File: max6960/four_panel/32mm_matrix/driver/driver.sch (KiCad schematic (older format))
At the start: 20 parts, among them M1 LED-MATRIX-8X8, M2 LED-MATRIX-8X8, M3 LED-MATRIX-8X8, M4 LED-MATRIX-8X8, P1 CONN_2X2, U1 MAX6960, U2 74AHC1G126, U3 MAX6960, U4 CONN15, U5 CONN15

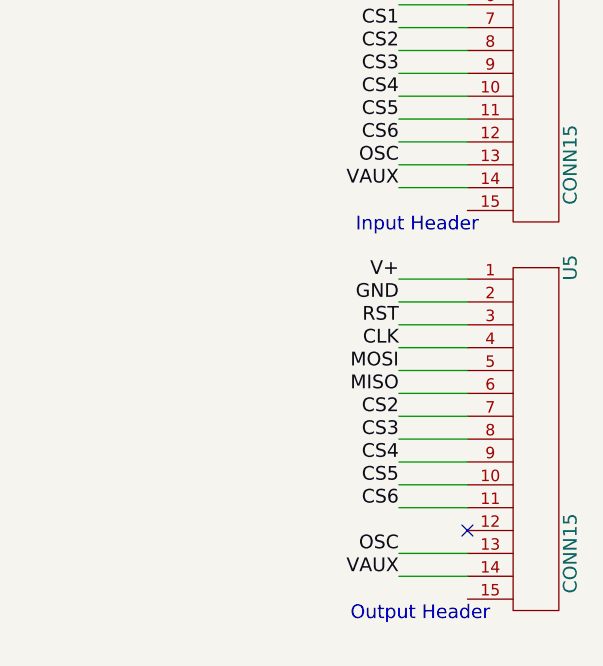
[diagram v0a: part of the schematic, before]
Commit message: Fixed errors in four panel 32mm matrix driver.
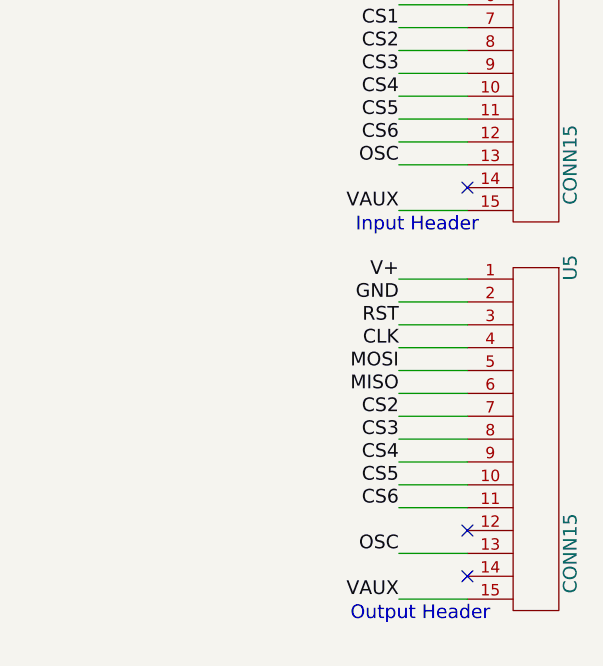
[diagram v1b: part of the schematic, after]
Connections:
- net VAUX: now also U4.15, U5.15; no longer U4.14, U5.14
- no-connect marks 2 -> 4
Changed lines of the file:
@@
-EESchema Schematic File Version 2  date Fri 26 Jul 2013 12:54:03 PM PDT
+EESchema Schematic File Version 2
 LIBS:power
 LIBS:device
@@
 LIBS:74ahc1g126
 LIBS:driver-cache
-EELAYER 25  0
+EELAYER 24 0
 EELAYER END
 $Descr User 18000 12000
@@
 	16100 7800 15800 7800
 Wire Wire Line
-	16100 7900 15800 7900
+	16100 8000 15800 8000
 Wire Wire Line
 	16100 8400 15800 8400
@@
 	16100 9200 15800 9200
 Wire Wire Line
-	16100 9600 15800 9600
+	16100 9700 15800 9700
 Wire Wire Line
 	11400 7450 10800 7450
@@
 F 0 "#PWR01" H 12850 9850 30  0001 C CNN
 F 1 "GND" H 12850 9780 30  0001 C CNN
+F 2 "" H 12850 9850 60  0001 C CNN
+F 3 "" H 12850 9850 60  0001 C CNN
 	1    12850 9850
 	1    0    0    -1
@@
 F 0 "P1" H 12300 9700 50  0000 C CNN
 F 1 "CONN_2X2" H 12310 9420 40  0000 C CNN
+F 2 "" H 12300 9550 60  0001 C CNN
+F 3 "" H 12300 9550 60  0001 C CNN
 	1    12300 9550
 	1    0    0    -1
@@
 F 0 "#PWR02" H 12850 8350 30  0001 C CNN
 F 1 "GND" H 12850 8280 30  0001 C CNN
+F 2 "" H 12850 8350 60  0001 C CNN
+F 3 "" H 12850 8350 60  0001 C CNN
 	1    12850 8350
 	1    0    0    -1
@@
 F 0 "C10" H 12900 8100 50  0000 L CNN
 F 1 "0.1uF" H 12900 7900 50  0000 L CNN
+F 2 "" H 12850 8000 60  0001 C CNN
+F 3 "" H 12850 8000 60  0001 C CNN
 	1    12850 8000
 	1    0    0    -1
@@
 F 0 "#PWR03" H 11250 7800 30  0001 C CNN
 F 1 "GND" H 11250 7730 30  0001 C CNN
+F 2 "" H 11250 7800 60  0001 C CNN
+F 3 "" H 11250 7800 60  0001 C CNN
 	1    11250 7800
 	1    0    0    -1
@@
 F 0 "U2" H 11750 7700 60  0000 C CNN
 F 1 "74AHC1G126" H 12000 7150 60  0000 C CNN
+F 2 "" H 12000 7450 60  0001 C CNN
+F 3 "" H 12000 7450 60  0001 C CNN
 	1    12000 7450
 	1    0    0    -1
 $EndComp
-Text Label 15800 9600 2    60   ~ 0
+Text Label 15800 9700 2    60   ~ 0
 VAUX
 Text Label 15800 9500 2    60   ~ 0
@@
 F 0 "U5" H 15550 9250 60  0000 C CNN
 F 1 "CONN15" H 16800 9250 60  0000 C CNN
+F 2 "" H 16300 9000 60  0001 C CNN
+F 3 "" H 16300 9000 60  0001 C CNN
 	1    16300 9000
 	0    1    1    0
 $EndComp
-Text Label 15800 7900 2    60   ~ 0
+Text Label 15800 8000 2    60   ~ 0
 VAUX
 Text Label 15800 7700 2    60   ~ 0
@@
 F 0 "U4" H 15550 7550 60  0000 C CNN
 F 1 "CONN15" H 16800 7550 60  0000 C CNN
+F 2 "" H 16300 7300 60  0001 C CNN
+F 3 "" H 16300 7300 60  0001 C CNN
 	1    16300 7300
 	0    1    1    0
@@
 F 0 "M3" H 7600 8050 60  0000 C CNN
 F 1 "LED-MATRIX-8X8" H 7900 6600 60  0000 C CNN
+F 2 "" H 7900 7350 60  0001 C CNN
+F 3 "" H 7900 7350 60  0001 C CNN
 	1    7900 7350
 	1    0    0    -1
@@
 F 0 "M4" H 7600 9800 60  0000 C CNN
 F 1 "LED-MATRIX-8X8" H 7900 8350 60  0000 C CNN
+F 2 "" H 7900 9100 60  0001 C CNN
+F 3 "" H 7900 9100 60  0001 C CNN
 	1    7900 9100
 	1    0    0    -1
@@
 F 0 "C6" H 14250 1750 50  0000 L CNN
 F 1 "0.1uF" H 14250 1550 50  0000 L CNN
+F 2 "" H 14200 1650 60  0001 C CNN
+F 3 "" H 14200 1650 60  0001 C CNN
 	1    14200 1650
 	1    0    0    -1
@@
 F 0 "C7" H 14650 1750 50  0000 L CNN
 F 1 "0.1uF" H 14650 1550 50  0000 L CNN
+F 2 "" H 14600 1650 60  0001 C CNN
+F 3 "" H 14600 1650 60  0001 C CNN
 	1    14600 1650
 	1    0    0    -1
@@
 F 0 "C8" H 15050 1750 50  0000 L CNN
 F 1 "0.1uF" H 15050 1550 50  0000 L CNN
+F 2 "" H 15000 1650 60  0001 C CNN
+F 3 "" H 15000 1650 60  0001 C CNN
 	1    15000 1650
 	1    0    0    -1
@@
 F 0 "C9" H 15450 1750 50  0000 L CNN
 F 1 "0.1uF" H 15450 1550 50  0000 L CNN
+F 2 "" H 15400 1650 60  0001 C CNN
+F 3 "" H 15400 1650 60  0001 C CNN
 	1    15400 1650
 	1    0    0    -1
@@
 F 0 "#PWR04" H 14800 2200 30  0001 C CNN
 F 1 "GND" H 14800 2130 30  0001 C CNN
+F 2 "" H 14800 2200 60  0001 C CNN
+F 3 "" H 14800 2200 60  0001 C CNN
 	1    14800 2200
 	1    0    0    -1
@@
 F 0 "U3" H 12050 3250 60  0000 C CNN
 F 1 "MAX6960" H 12050 3400 60  0000 C CNN
+F 2 "" H 12050 3350 60  0001 C CNN
+F 3 "" H 12050 3350 60  0001 C CNN
 	1    12050 3350
 	1    0    0    -1
@@
 F 0 "#PWR05" H 11300 1400 30  0001 C CNN
 F 1 "GND" H 11300 1330 30  0001 C CNN
+F 2 "" H 11300 1400 60  0001 C CNN
+F 3 "" H 11300 1400 60  0001 C CNN
 	1    11300 1400
 	1    0    0    -1
@@
 F 0 "#PWR06" H 9800 4250 30  0001 C CNN
 F 1 "GND" H 9800 4180 30  0001 C CNN
+F 2 "" H 9800 4250 60  0001 C CNN
+F 3 "" H 9800 4250 60  0001 C CNN
 	1    9800 4250
 	1    0    0    -1
@@
 F 0 "#PWR07" H 9800 3500 30  0001 C CNN
 F 1 "GND" H 9800 3430 30  0001 C CNN
+F 2 "" H 9800 3500 60  0001 C CNN
+F 3 "" H 9800 3500 60  0001 C CNN
 	1    9800 3500
 	1    0    0    -1
@@
 F 0 "#PWR08" H 9800 2750 30  0001 C CNN
 F 1 "GND" H 9800 2680 30  0001 C CNN
+F 2 "" H 9800 2750 60  0001 C CNN
+F 3 "" H 9800 2750 60  0001 C CNN
 	1    9800 2750
 	1    0    0    -1
@@
 F 0 "#PWR09" H 11300 5100 30  0001 C CNN
 F 1 "GND" H 11300 5030 30  0001 C CNN
+F 2 "" H 11300 5100 60  0001 C CNN
+F 3 "" H 11300 5100 60  0001 C CNN
 	1    11300 5100
 	1    0    0    -1
@@
 F 0 "#PWR010" H 1900 1750 30  0001 C CNN
 F 1 "GND" H 1900 1680 30  0001 C CNN
+F 2 "" H 1900 1750 60  0001 C CNN
+F 3 "" H 1900 1750 60  0001 C CNN
 	1    1900 1750
 	1    0    0    -1
@@
 F 0 "#FLG011" H 1900 1720 30  0001 C CNN
 F 1 "PWR_FLAG" H 1900 1680 30  0000 C CNN
+F 2 "" H 1900 1450 60  0001 C CNN
+F 3 "" H 1900 1450 60  0001 C CNN
 	1    1900 1450
 	1    0    0    -1
@@
 F 0 "#FLG012" H 1550 1720 30  0001 C CNN
 F 1 "PWR_FLAG" H 1550 1680 30  0000 C CNN
+F 2 "" H 1550 1450 60  0001 C CNN
+F 3 "" H 1550 1450 60  0001 C CNN
 	1    1550 1450
 	1    0    0    -1
@@
 F 0 "M2" H 2900 9750 60  0000 C CNN
 F 1 "LED-MATRIX-8X8" H 3200 8300 60  0000 C CNN
+F 2 "" H 3200 9050 60  0001 C CNN
+F 3 "" H 3200 9050 60  0001 C CNN
 	1    3200 9050
 	1    0    0    -1
@@
 F 0 "M1" H 2900 8000 60  0000 C CNN
 F 1 "LED-MATRIX-8X8" H 3200 6550 60  0000 C CNN
+F 2 "" H 3200 7300 60  0001 C CNN
+F 3 "" H 3200 7300 60  0001 C CNN
 	1    3200 7300
 	1    0    0    -1
@@
 F 0 "#PWR013" H 3300 5150 30  0001 C CNN
 F 1 "GND" H 3300 5080 30  0001 C CNN
+F 2 "" H 3300 5150 60  0001 C CNN
+F 3 "" H 3300 5150 60  0001 C CNN
 	1    3300 5150
 	1    0    0    -1
@@
 F 0 "#PWR014" H 1800 2800 30  0001 C CNN
 F 1 "GND" H 1800 2730 30  0001 C CNN
+F 2 "" H 1800 2800 60  0001 C CNN
+F 3 "" H 1800 2800 60  0001 C CNN
 	1    1800 2800
 	1    0    0    -1
@@
 F 0 "#PWR015" H 1800 3550 30  0001 C CNN
 F 1 "GND" H 1800 3480 30  0001 C CNN
+F 2 "" H 1800 3550 60  0001 C CNN
+F 3 "" H 1800 3550 60  0001 C CNN
 	1    1800 3550
 	1    0    0    -1
@@
 F 0 "#PWR016" H 1800 4300 30  0001 C CNN
 F 1 "GND" H 1800 4230 30  0001 C CNN
+F 2 "" H 1800 4300 60  0001 C CNN
+F 3 "" H 1800 4300 60  0001 C CNN
 	1    1800 4300
 	1    0    0    -1
@@
 F 0 "#PWR017" H 3300 1450 30  0001 C CNN
 F 1 "GND" H 3300 1380 30  0001 C CNN
+F 2 "" H 3300 1450 60  0001 C CNN
+F 3 "" H 3300 1450 60  0001 C CNN
 	1    3300 1450
 	1    0    0    -1
@@
 F 0 "#PWR018" H 6500 2250 30  0001 C CNN
 F 1 "GND" H 6500 2180 30  0001 C CNN
+F 2 "" H 6500 2250 60  0001 C CNN
+F 3 "" H 6500 2250 60  0001 C CNN
 	1    6500 2250
 	1    0    0    -1
@@
 F 0 "C5" H 7350 1800 50  0000 L CNN
 F 1 "0.1uF" H 7350 1600 50  0000 L CNN
+F 2 "" H 7300 1700 60  0001 C CNN
+F 3 "" H 7300 1700 60  0001 C CNN
 	1    7300 1700
 	1    0    0    -1
@@
 F 0 "C4" H 6950 1800 50  0000 L CNN
 F 1 "0.1uF" H 6950 1600 50  0000 L CNN
+F 2 "" H 6900 1700 60  0001 C CNN
+F 3 "" H 6900 1700 60  0001 C CNN
 	1    6900 1700
 	1    0    0    -1
@@
 F 0 "C3" H 6550 1800 50  0000 L CNN
 F 1 "0.1uF" H 6550 1600 50  0000 L CNN
+F 2 "" H 6500 1700 60  0001 C CNN
+F 3 "" H 6500 1700 60  0001 C CNN
 	1    6500 1700
 	1    0    0    -1
@@
 F 0 "C2" H 6150 1800 50  0000 L CNN
 F 1 "0.1uF" H 6150 1600 50  0000 L CNN
+F 2 "" H 6100 1700 60  0001 C CNN
+F 3 "" H 6100 1700 60  0001 C CNN
 	1    6100 1700
 	1    0    0    -1
@@
 F 0 "C1" H 5700 1800 50  0000 L CNN
 F 1 "47uF" H 5700 1600 50  0000 L CNN
+F 2 "" H 5650 1700 60  0001 C CNN
+F 3 "" H 5650 1700 60  0001 C CNN
 	1    5650 1700
 	1    0    0    -1
@@
 F 0 "U1" H 4050 3300 60  0000 C CNN
 F 1 "MAX6960" H 4050 3450 60  0000 C CNN
+F 2 "" H 4050 3400 60  0001 C CNN
+F 3 "" H 4050 3400 60  0001 C CNN
 	1    4050 3400
 	1    0    0    -1
 $EndComp
+NoConn ~ 16100 7900
+NoConn ~ 16100 9600
 $EndSCHEMATC
